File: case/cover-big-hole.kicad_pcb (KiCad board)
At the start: 2 copper layers, 20.5 x 57.2 mm, 4 parts

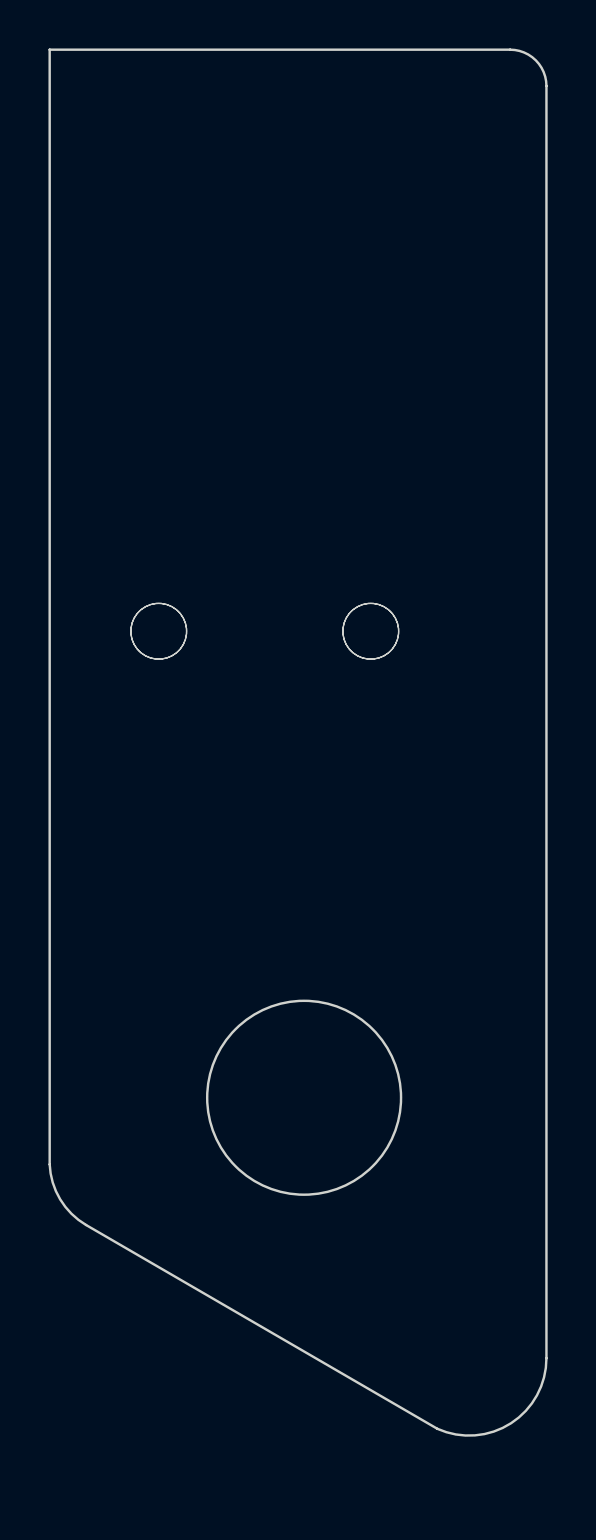
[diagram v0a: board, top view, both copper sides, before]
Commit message: adjust top plate, add new cover in PCB style
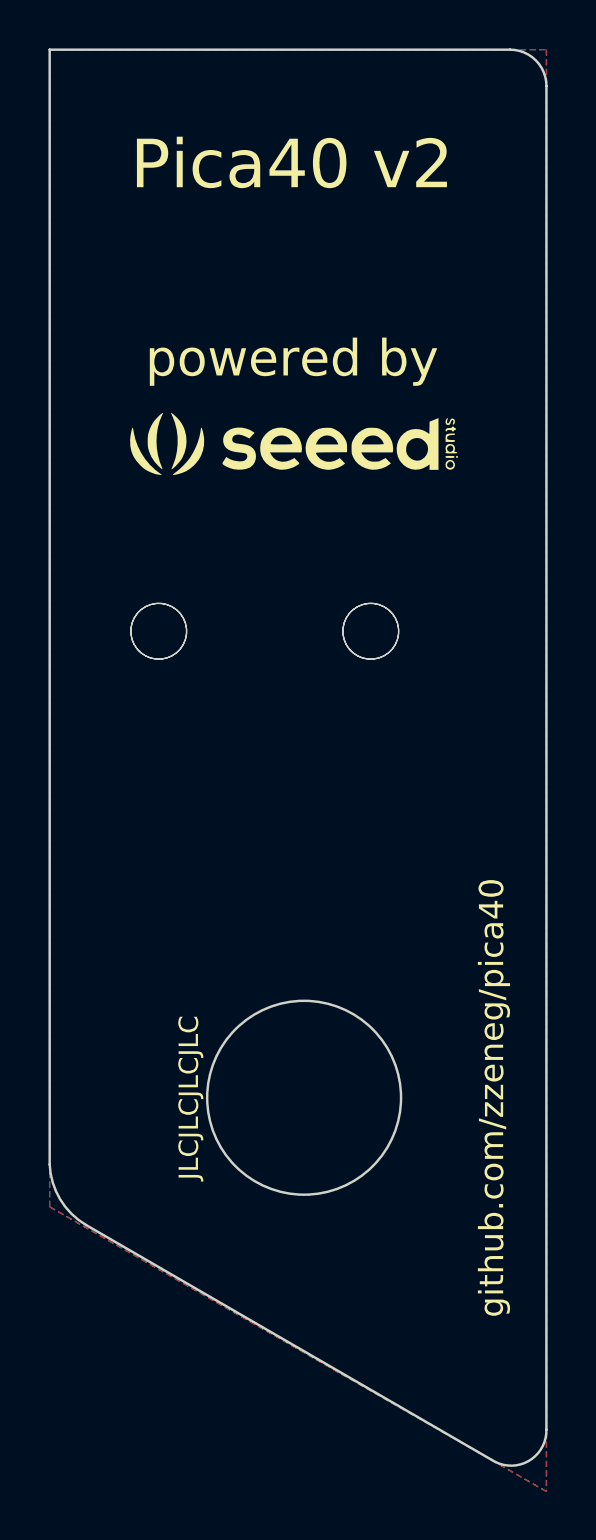
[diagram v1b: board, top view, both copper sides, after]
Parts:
- added G***: LOGO, pica:seeed-logo, F.Cu at (135.5, 76.2)
- added G***: LOGO, pica:seeed-logo, B.Cu at (135.5, 76.2)
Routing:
- added copper zone on B.Cu, net (none)
- added copper zone on F.Cu, net (none)
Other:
- board size 20.5 x 57.2 mm -> 20.5 x 58.4 mm
- board text added: "JLCJLCJLCJLC"
- board text added: "Pica40 v2"
- board text added: "github.com/zzeneg/pica40"
- board text added: "powered by"
